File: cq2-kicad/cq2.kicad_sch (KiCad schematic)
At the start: 34 parts, among them J1 Pin Header, P2 Pin Header, P3 Terminal Header w/ flanges

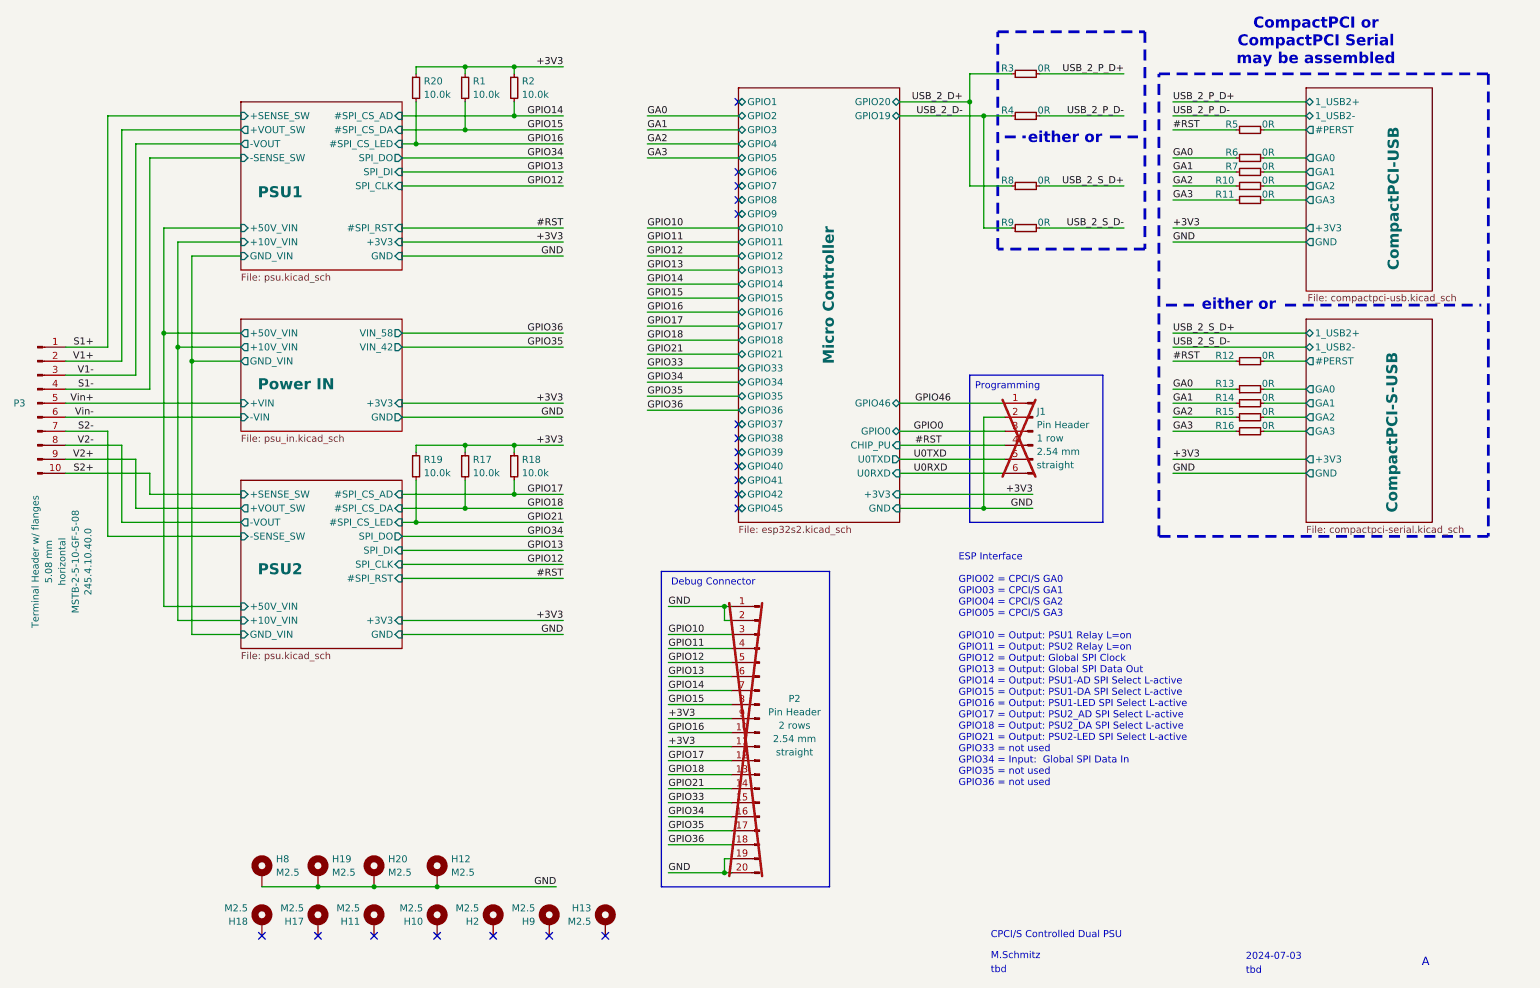
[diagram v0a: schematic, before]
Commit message: drc checked before panalization
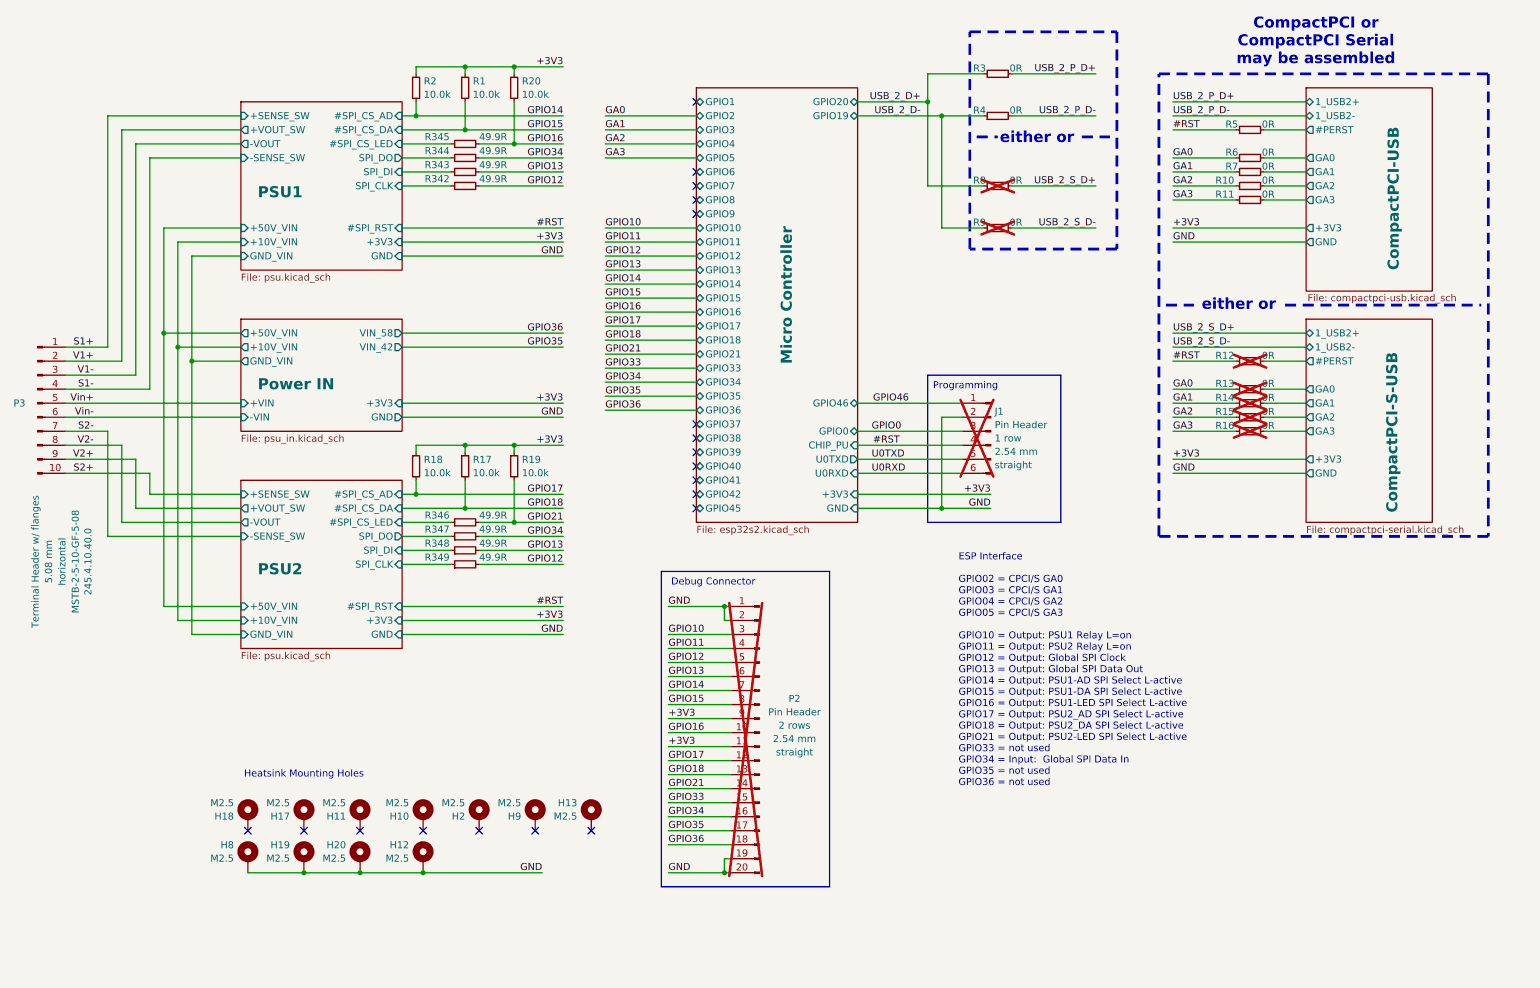
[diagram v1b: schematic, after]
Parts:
- added R342, R343, R344, R345, R346, R347, R348, R349: 49.9R, 0-standard:0402-resistor, symbol ci4rail-database:resistors/117
- R12, R13, R14, R15, R16, R8, R9: now not fitted
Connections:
- net GPIO12: now also R342.2, R349.2
- net GPIO13: now also R343.2, R348.2
- net GPIO16: now also R345.2
- net GPIO21: now also R346.2
- net GPIO34: now also R344.2, R347.2
- new net PSU1/#SPI_CS_LED: R345.1
- new net PSU1/SPI_CLK: R342.1
- new net PSU1/SPI_DI: R343.1
- new net PSU1/SPI_DO: R344.1
- new net PSU2/#SPI_CS_LED: R346.1
- new net PSU2/SPI_CLK: R349.1
- new net PSU2/SPI_DI: R348.1
- new net PSU2/SPI_DO: R347.1
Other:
- note added: "Heatsink Mounting Holes"
- note removed: "2024-07-03"
- note removed: "A"
- note removed: "CPCI/S Controlled Dual PSU"
- note removed: "M.Schmitz"
- note removed: "tbd"
- moved on the sheet: H10, H11, H12, H13, H17, H18, H19, H2, H20, H8, H9, J1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
